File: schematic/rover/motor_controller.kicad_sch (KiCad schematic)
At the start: 6 parts

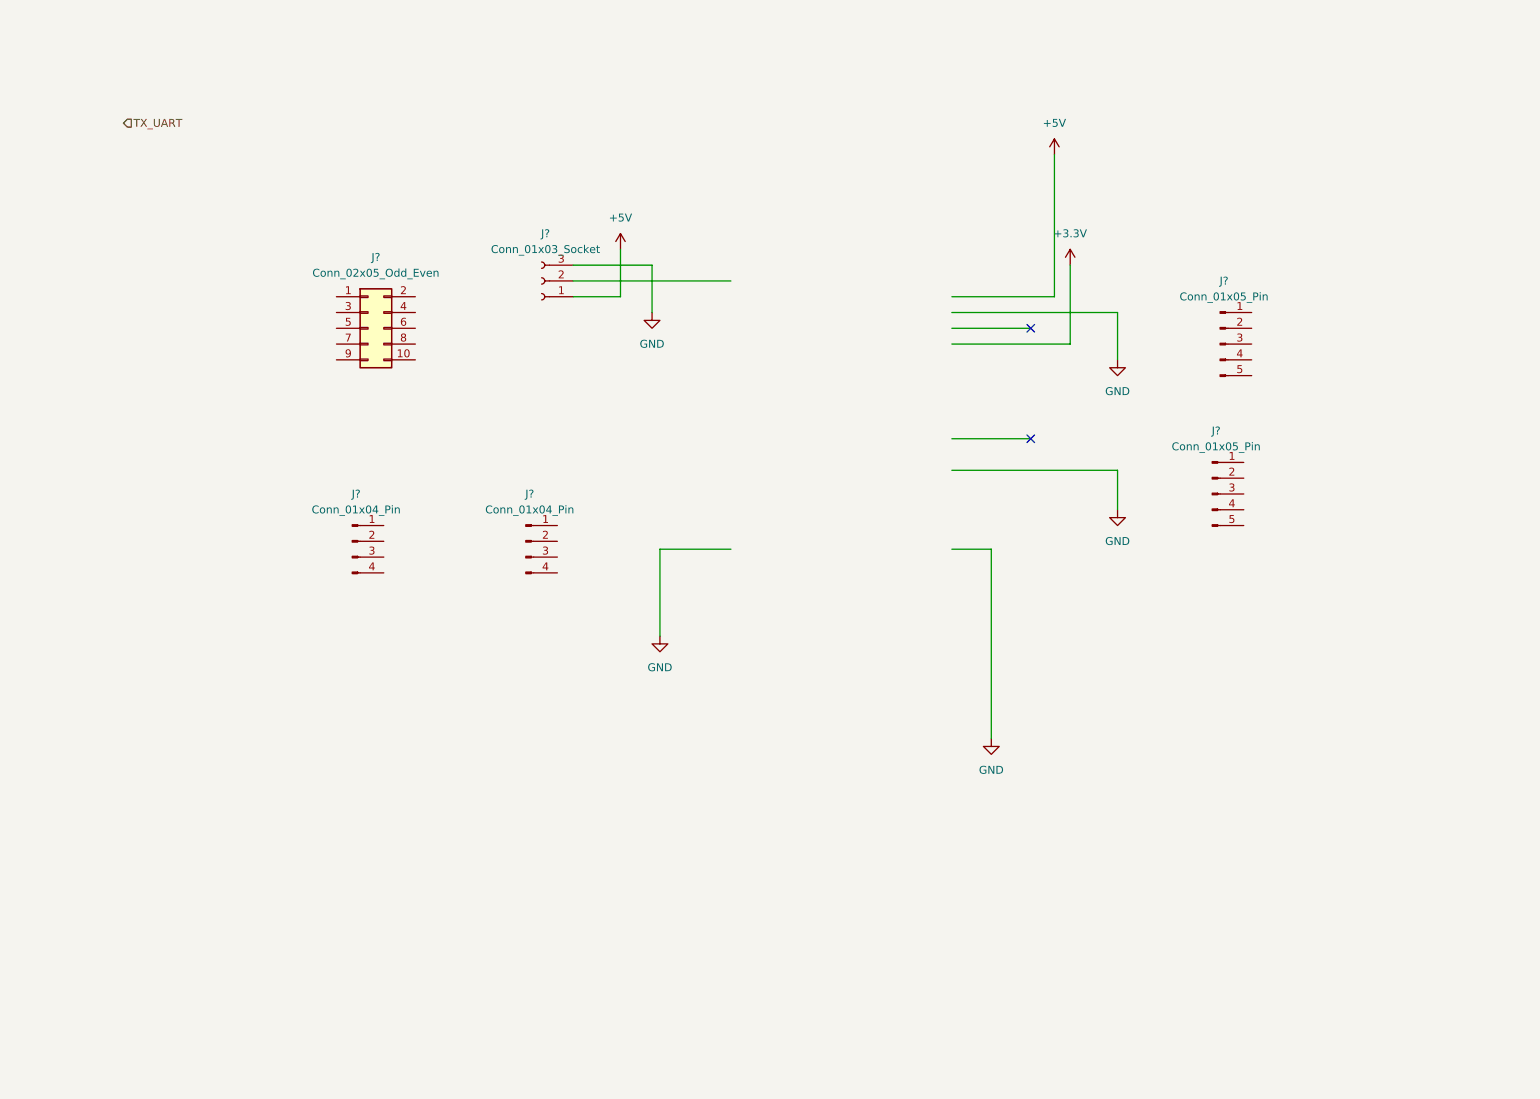
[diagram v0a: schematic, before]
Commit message: Complete motor controller schematic
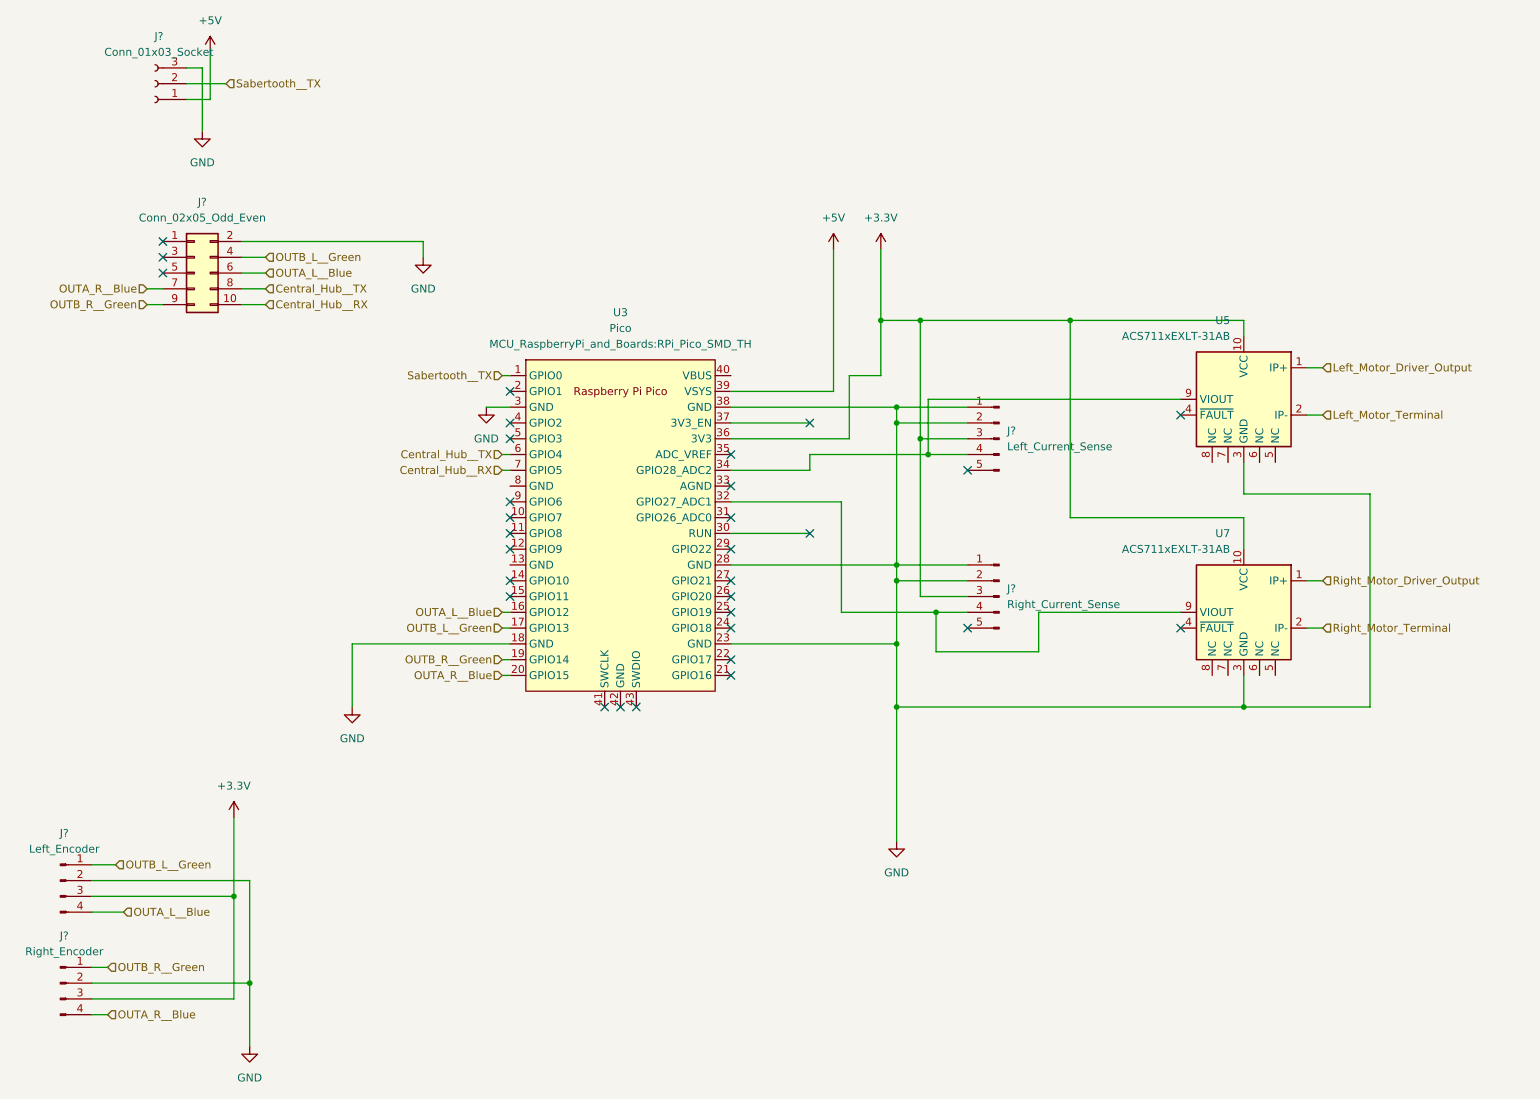
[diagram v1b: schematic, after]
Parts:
- removed J?: Conn_01x03_Socket, Connector_PinHeader_2.54mm:PinHeader_1x03_P2.54mm_Vertical, symbol Connector:Conn_01x03_Socket
- added J?: Conn_01x03_Socket, Connector_PinHeader_2.54mm:PinHeader_1x03_P2.54mm_Vertical, symbol Connector:Conn_01x03_Socket
- added U3: Pico, MCU_RaspberryPi_and_Boards:RPi_Pico_SMD_TH, symbol MCU_RaspberryPi_and_Boards:Pico
- added U5, U7: ACS711xEXLT-31AB, Sensor_Current:Allegro_QFN-12-10-1EP_3x3mm_P0.5mm, symbol Sensor_Current:ACS711xEXLT-31AB
- J?: value Conn_01x04_Pin -> Left_Encoder
- J?: value Conn_01x05_Pin -> Left_Current_Sense
- J?: value Conn_01x04_Pin -> Right_Encoder
- J?: value Conn_01x05_Pin -> Right_Current_Sense
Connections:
- net +3.3V: now also J?.3 (Pin_3), J?.3 (Pin_3), J?.3 (Pin_3), J?.3 (Pin_3), U3.36 (3V3), U5.10 (VCC), U7.10 (VCC)
- net +5V: now also J?.1 (Pin_1), U3.39 (VSYS)
- net GND: now also J?.1 (Pin_1), J?.1 (Pin_1), J?.2 (Pin_2), J?.2 (Pin_2), J?.2 (Pin_2), J?.2 (Pin_2), J?.2 (Pin_2), J?.3 (Pin_3), U3.18 (GND), U3.23 (GND), U3.28 (GND), U3.3 (GND), U3.38 (GND), U5.3 (GND), U7.3 (GND)
- net OUTB_L__Green: now reaches J?.1 (Pin_1)
- net OUTB_L__Green: now also J?.4 (Pin_4), U3.17 (GPIO13)
- net OUTA_L__Blue: now reaches J?.4 (Pin_4)
- net OUTA_L__Blue: now also J?.6 (Pin_6), U3.16 (GPIO12)
- net at J?.4 (Pin_4): now also U3.34 (GPIO28_ADC2), U5.9 (VIOUT)
- net OUTB_R__Green: now reaches J?.1 (Pin_1)
- net OUTB_R__Green: now also J?.9 (Pin_9), U3.19 (GPIO14)
- net OUTA_R__Blue: now reaches J?.4 (Pin_4)
- net OUTA_R__Blue: now also J?.7 (Pin_7), U3.20 (GPIO15)
- net at J?.4 (Pin_4): now also U3.32 (GPIO27_ADC1), U7.9 (VIOUT)
- net Central_Hub__RX: now reaches J?.10 (Pin_10)
- net Central_Hub__RX: now also U3.7 (GPIO5)
- net Central_Hub__TX: now reaches J?.8 (Pin_8)
- net Central_Hub__TX: now also U3.6 (GPIO4)
- new net Left_Motor_Driver_Output: U5.1 (IP+)
- new net Left_Motor_Terminal: U5.2 (IP-)
- new net Right_Motor_Driver_Output: U7.1 (IP+)
- new net Right_Motor_Terminal: U7.2 (IP-)
- new net Sabertooth__TX: J?.2 (Pin_2), U3.1 (GPIO0)
- no-connect marks 2 -> 31
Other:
- moved on the sheet: J?

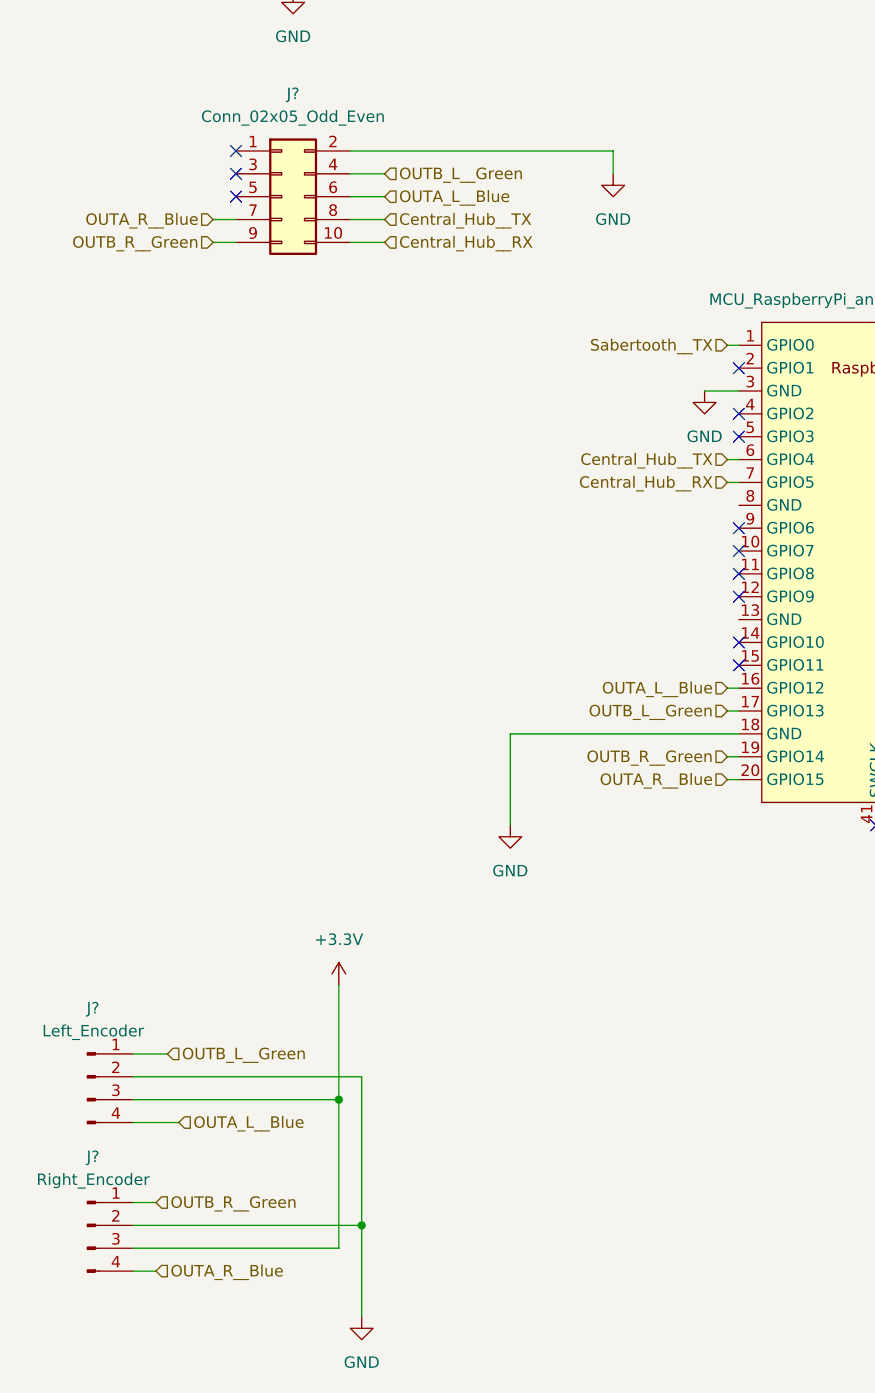
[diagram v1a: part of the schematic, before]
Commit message: Update connection between picos
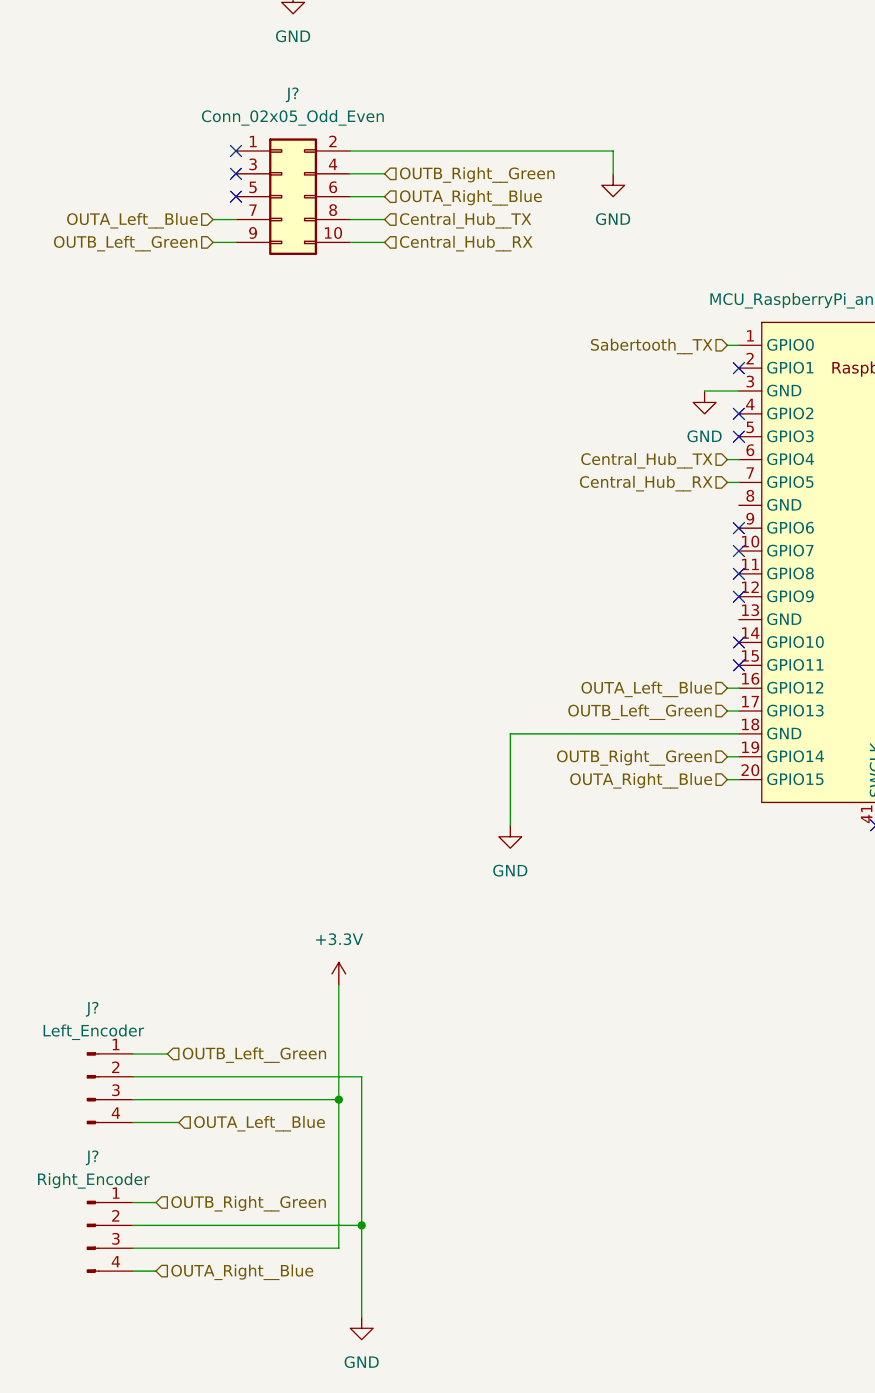
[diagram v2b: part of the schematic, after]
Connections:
- net OUTA_L__Blue renamed OUTA_Left__Blue
- net OUTA_Left__Blue: now also J?.7 (Pin_7); no longer J?.6 (Pin_6)
- net OUTA_R__Blue renamed OUTA_Right__Blue
- net OUTA_Right__Blue: now also J?.6 (Pin_6); no longer J?.7 (Pin_7)
- net OUTB_L__Green renamed OUTB_Left__Green
- net OUTB_Left__Green: now also J?.9 (Pin_9); no longer J?.4 (Pin_4)
- net OUTB_R__Green renamed OUTB_Right__Green
- net OUTB_Right__Green: now also J?.4 (Pin_4); no longer J?.9 (Pin_9)
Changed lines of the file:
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@@
     (effects (font (size 1.27 1.27)) (justify left))
   )
-  (hierarchical_label "OUTA_L__Blue" (shape input) (at 58.42 62.23 0) (fields_autoplaced)
+  (hierarchical_label "OUTA_Right__Blue" (shape input) (at 58.42 62.23 0) (fields_autoplaced)
     (effects (font (size 1.27 1.27)) (justify left))
   )
-  (hierarchical_label "OUTA_L__Blue" (shape input) (at 96.52 116.84 180) (fields_autoplaced)
+  (hierarchical_label "OUTA_Left__Blue" (shape input) (at 96.52 116.84 180) (fields_autoplaced)
     (effects (font (size 1.27 1.27)) (justify right))
   )
@@
     (effects (font (size 1.27 1.27)) (justify right))
   )
-  (hierarchical_label "OUTB_L__Green" (shape input) (at 34.29 157.48 0) (fields_autoplaced)
+  (hierarchical_label "OUTB_Left__Green" (shape input) (at 34.29 157.48 0) (fields_autoplaced)
     (effects (font (size 1.27 1.27)) (justify left))
   )
@@
     (effects (font (size 1.27 1.27)) (justify left))
   )
-  (hierarchical_label "OUTB_R__Green" (shape input) (at 39.37 67.31 180) (fields_autoplaced)
+  (hierarchical_label "OUTB_Left__Green" (shape input) (at 39.37 67.31 180) (fields_autoplaced)
     (effects (font (size 1.27 1.27)) (justify right))
   )
-  (hierarchical_label "OUTB_L__Green" (shape input) (at 96.52 119.38 180) (fields_autoplaced)
+  (hierarchical_label "OUTB_Left__Green" (shape input) (at 96.52 119.38 180) (fields_autoplaced)
     (effects (font (size 1.27 1.27)) (justify right))
   )
@@
     (effects (font (size 1.27 1.27)) (justify left))
   )
-  (hierarchical_label "OUTB_R__Green" (shape input) (at 33.02 173.99 0) (fields_autoplaced)
+  (hierarchical_label "OUTB_Right__Green" (shape input) (at 33.02 173.99 0) (fields_autoplaced)
     (effects (font (size 1.27 1.27)) (justify left))
   )
-  (hierarchical_label "OUTA_R__Blue" (shape input) (at 33.02 181.61 0) (fields_autoplaced)
+  (hierarchical_label "OUTA_Right__Blue" (shape input) (at 33.02 181.61 0) (fields_autoplaced)
     (effects (font (size 1.27 1.27)) (justify left))
   )
-  (hierarchical_label "OUTA_R__Blue" (shape input) (at 96.52 127 180) (fields_autoplaced)
+  (hierarchical_label "OUTA_Right__Blue" (shape input) (at 96.52 127 180) (fields_autoplaced)
     (effects (font (size 1.27 1.27)) (justify right))
   )
-  (hierarchical_label "OUTA_L__Blue" (shape input) (at 35.56 165.1 0) (fields_autoplaced)
+  (hierarchical_label "OUTA_Left__Blue" (shape input) (at 35.56 165.1 0) (fields_autoplaced)
     (effects (font (size 1.27 1.27)) (justify left))
   )
-  (hierarchical_label "OUTB_L__Green" (shape input) (at 58.42 59.69 0) (fields_autoplaced)
+  (hierarchical_label "OUTB_Right__Green" (shape input) (at 58.42 59.69 0) (fields_autoplaced)
     (effects (font (size 1.27 1.27)) (justify left))
   )
-  (hierarchical_label "OUTB_R__Green" (shape input) (at 96.52 124.46 180) (fields_autoplaced)
+  (hierarchical_label "OUTB_Right__Green" (shape input) (at 96.52 124.46 180) (fields_autoplaced)
     (effects (font (size 1.27 1.27)) (justify right))
   )
@@
     (effects (font (size 1.27 1.27)) (justify right))
   )
-  (hierarchical_label "OUTA_R__Blue" (shape input) (at 39.37 64.77 180) (fields_autoplaced)
+  (hierarchical_label "OUTA_Left__Blue" (shape input) (at 39.37 64.77 180) (fields_autoplaced)
     (effects (font (size 1.27 1.27)) (justify right))
   )
